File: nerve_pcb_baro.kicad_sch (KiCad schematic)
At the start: 5 parts, among them U4 BMP390

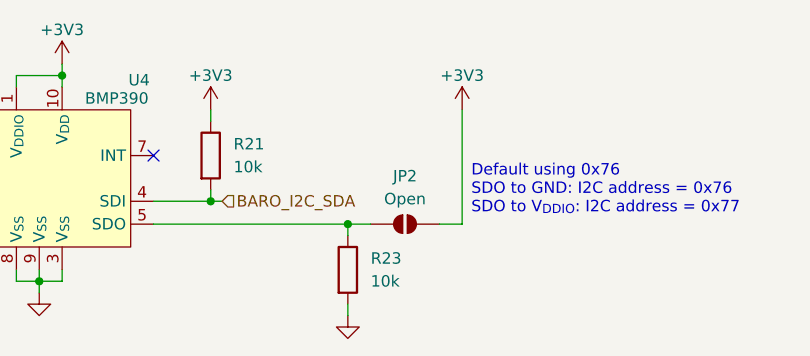
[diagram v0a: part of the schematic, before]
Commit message: Cleanup Vbatt circuit and fix silkscreen
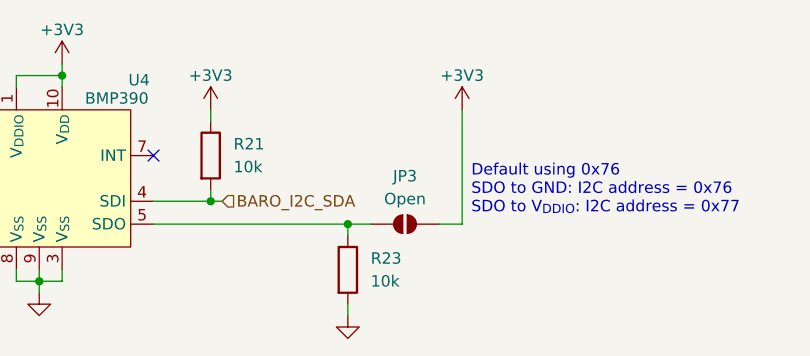
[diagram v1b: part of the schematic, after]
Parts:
- renumbered JP2 to JP3
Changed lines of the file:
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@@
 		(dnp no)
 		(fields_autoplaced yes)
-		(property "Reference" "#PWR074"
+		(property "Reference" "#PWR076"
 			(at 137.16 115.57 0)
 			(effects
@@
 			(project "nerve_pcb"
 				(path "/c0277862-b3f2-4e0e-986f-34702f0543f0/9de129d2-0f7b-4a2d-85ad-214e335f6288"
-					(reference "#PWR074")
+					(reference "#PWR076")
 					(unit 1)
 				)
@@
 		(on_board yes)
 		(dnp no)
-		(property "Reference" "#PWR071"
+		(property "Reference" "#PWR073"
 			(at 184.15 92.71 0)
 			(effects
@@
 			(project "nerve_pcb"
 				(path "/c0277862-b3f2-4e0e-986f-34702f0543f0/9de129d2-0f7b-4a2d-85ad-214e335f6288"
-					(reference "#PWR071")
+					(reference "#PWR073")
 					(unit 1)
 				)
@@
 		(on_board yes)
 		(dnp no)
-		(property "Reference" "#PWR070"
+		(property "Reference" "#PWR072"
 			(at 156.21 92.71 0)
 			(effects
@@
 			(project "nerve_pcb"
 				(path "/c0277862-b3f2-4e0e-986f-34702f0543f0/9de129d2-0f7b-4a2d-85ad-214e335f6288"
-					(reference "#PWR070")
+					(reference "#PWR072")
 					(unit 1)
 				)
@@
 		(on_board yes)
 		(dnp no)
-		(property "Reference" "JP2"
+		(property "Reference" "JP3"
 			(at 177.8 96.266 0)
 			(effects
@@
 			(project "nerve_pcb"
 				(path "/c0277862-b3f2-4e0e-986f-34702f0543f0/9de129d2-0f7b-4a2d-85ad-214e335f6288"
-					(reference "JP2")
+					(reference "JP3")
 					(unit 1)
 				)
@@
 		(on_board yes)
 		(dnp no)
-		(property "Reference" "#PWR069"
+		(property "Reference" "#PWR071"
 			(at 139.7 87.63 0)
 			(effects
@@
 			(project "nerve_pcb"
 				(path "/c0277862-b3f2-4e0e-986f-34702f0543f0/9de129d2-0f7b-4a2d-85ad-214e335f6288"
-					(reference "#PWR069")
+					(reference "#PWR071")
 					(unit 1)
 				)
@@
 		(on_board yes)
 		(dnp no)
-		(property "Reference" "#PWR072"
+		(property "Reference" "#PWR074"
 			(at 123.19 96.52 0)
 			(effects
@@
 			(project "nerve_pcb"
 				(path "/c0277862-b3f2-4e0e-986f-34702f0543f0/9de129d2-0f7b-4a2d-85ad-214e335f6288"
-					(reference "#PWR072")
+					(reference "#PWR074")
 					(unit 1)
 				)
@@
 		(on_board yes)
 		(dnp no)
-		(property "Reference" "#PWR073"
+		(property "Reference" "#PWR075"
 			(at 114.3 100.33 0)
 			(effects
@@
 			(project "nerve_pcb"
 				(path "/c0277862-b3f2-4e0e-986f-34702f0543f0/9de129d2-0f7b-4a2d-85ad-214e335f6288"
-					(reference "#PWR073")
+					(reference "#PWR075")
 					(unit 1)
 				)
@@
 		(dnp no)
 		(fields_autoplaced yes)
-		(property "Reference" "#PWR075"
+		(property "Reference" "#PWR077"
 			(at 171.45 118.11 0)
 			(effects
@@
 			(project "nerve_pcb"
 				(path "/c0277862-b3f2-4e0e-986f-34702f0543f0/9de129d2-0f7b-4a2d-85ad-214e335f6288"
-					(reference "#PWR075")
-					(unit 1)
-				)
+					(reference "#PWR077")
+					(unit 1)
+				)

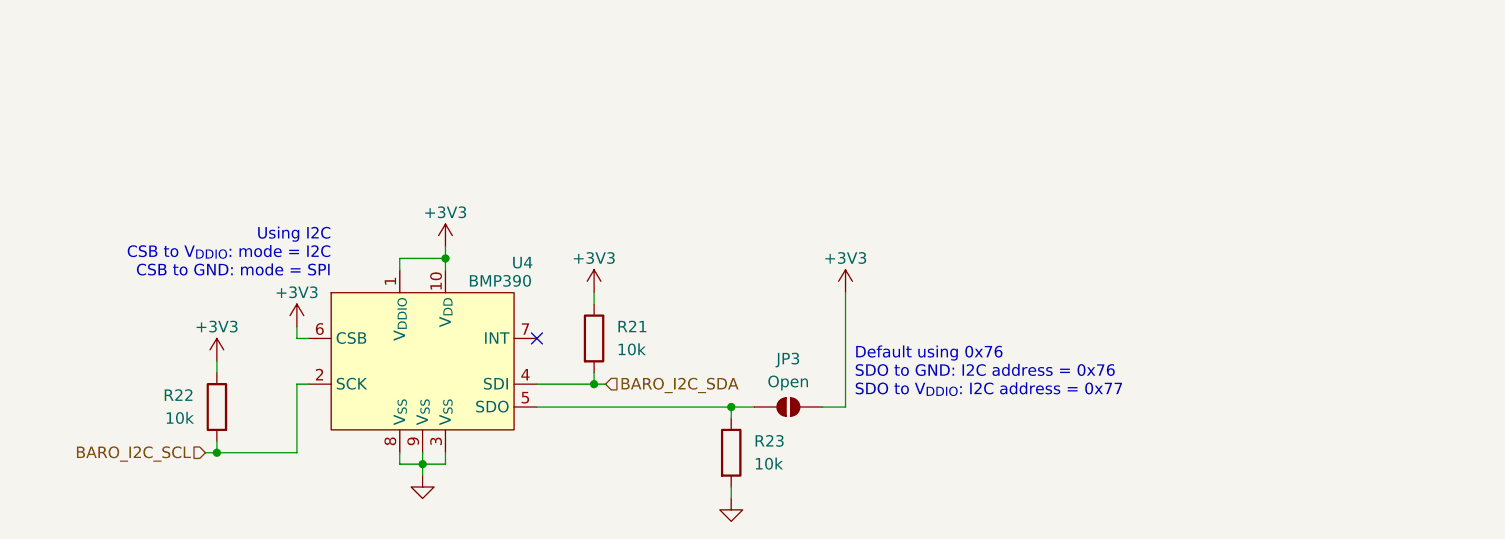
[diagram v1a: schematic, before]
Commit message: Schematic corrections
- Add decoupling caps for sensor ICs
- Fix clock circuits
- Add BNO085 clock jumper
- Minor cleanup
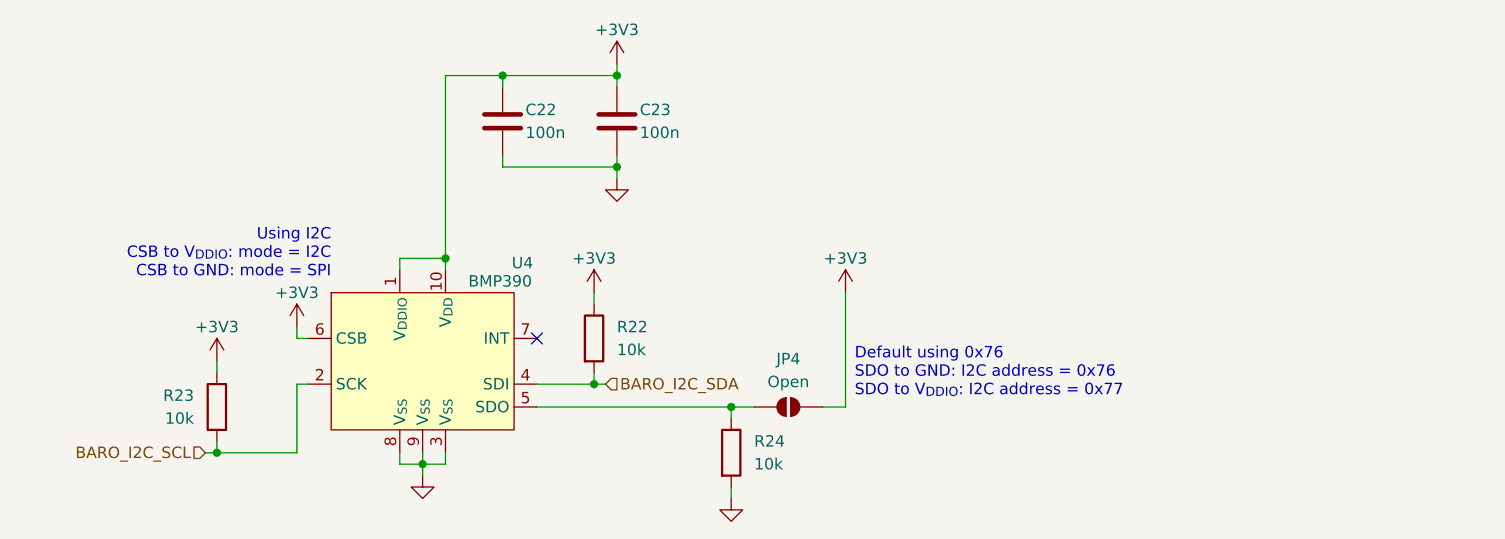
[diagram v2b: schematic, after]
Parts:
- added C22, C23: 100n, Capacitor_SMD:C_0603_1608Metric, symbol Device:C
- renumbered JP3 to JP4, R21 to R22, R22 to R23, R23 to R24
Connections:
- net +3V3: now also C22.1, C23.1
- net GND: now also C22.2, C23.2

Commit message: Simplify clock circuits
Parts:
- renumbered R22 to R19, R23 to R20, R24 to R21
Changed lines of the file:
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@@
 		(on_board yes)
 		(dnp no)
-		(property "Reference" "R22"
+		(property "Reference" "R19"
 			(at 158.75 92.7099 0)
 			(effects
@@
 			(project "nerve_pcb"
 				(path "/c0277862-b3f2-4e0e-986f-34702f0543f0/9de129d2-0f7b-4a2d-85ad-214e335f6288"
-					(reference "R22")
+					(reference "R19")
 					(unit 1)
 				)
@@
 		(on_board yes)
 		(dnp no)
-		(property "Reference" "R23"
+		(property "Reference" "R20"
 			(at 111.76 100.3299 0)
 			(effects
@@
 			(project "nerve_pcb"
 				(path "/c0277862-b3f2-4e0e-986f-34702f0543f0/9de129d2-0f7b-4a2d-85ad-214e335f6288"
-					(reference "R23")
+					(reference "R20")
 					(unit 1)
 				)
@@
 		(on_board yes)
 		(dnp no)
-		(property "Reference" "R24"
+		(property "Reference" "R21"
 			(at 173.99 105.4099 0)
 			(effects
@@
 			(project "nerve_pcb"
 				(path "/c0277862-b3f2-4e0e-986f-34702f0543f0/9de129d2-0f7b-4a2d-85ad-214e335f6288"
-					(reference "R24")
-					(unit 1)
-				)
+					(reference "R21")
+					(unit 1)
+				)

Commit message: Update IMU clock circuit and cleanup
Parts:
- renumbered R19 to R17, R20 to R18, R21 to R19
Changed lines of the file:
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@@
 		(on_board yes)
 		(dnp no)
-		(property "Reference" "R19"
+		(property "Reference" "R17"
 			(at 158.75 92.7099 0)
 			(effects
@@
 			(project "nerve_pcb"
 				(path "/c0277862-b3f2-4e0e-986f-34702f0543f0/9de129d2-0f7b-4a2d-85ad-214e335f6288"
-					(reference "R19")
+					(reference "R17")
 					(unit 1)
 				)
@@
 		(on_board yes)
 		(dnp no)
-		(property "Reference" "R20"
+		(property "Reference" "R18"
 			(at 111.76 100.3299 0)
 			(effects
@@
 			(project "nerve_pcb"
 				(path "/c0277862-b3f2-4e0e-986f-34702f0543f0/9de129d2-0f7b-4a2d-85ad-214e335f6288"
-					(reference "R20")
+					(reference "R18")
 					(unit 1)
 				)
@@
 		(on_board yes)
 		(dnp no)
-		(property "Reference" "R21"
+		(property "Reference" "R19"
 			(at 173.99 105.4099 0)
 			(effects
@@
 			(project "nerve_pcb"
 				(path "/c0277862-b3f2-4e0e-986f-34702f0543f0/9de129d2-0f7b-4a2d-85ad-214e335f6288"
-					(reference "R21")
-					(unit 1)
-				)
+					(reference "R19")
+					(unit 1)
+				)

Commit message: Add WS2812Bs
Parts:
- renumbered U4 to U5
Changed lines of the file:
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@@
 		(dnp no)
 		(fields_autoplaced yes)
-		(property "Reference" "#PWR069"
+		(property "Reference" "#PWR076"
 			(at 137.16 115.57 0)
 			(effects
@@
 			(project "nerve_pcb"
 				(path "/c0277862-b3f2-4e0e-986f-34702f0543f0/9de129d2-0f7b-4a2d-85ad-214e335f6288"
-					(reference "#PWR069")
+					(reference "#PWR076")
 					(unit 1)
 				)
@@
 		(on_board yes)
 		(dnp no)
-		(property "Reference" "#PWR066"
+		(property "Reference" "#PWR073"
 			(at 184.15 92.71 0)
 			(effects
@@
 			(project "nerve_pcb"
 				(path "/c0277862-b3f2-4e0e-986f-34702f0543f0/9de129d2-0f7b-4a2d-85ad-214e335f6288"
-					(reference "#PWR066")
+					(reference "#PWR073")
 					(unit 1)
 				)
@@
 		(on_board yes)
 		(dnp no)
-		(property "Reference" "#PWR065"
+		(property "Reference" "#PWR072"
 			(at 156.21 92.71 0)
 			(effects
@@
 			(project "nerve_pcb"
 				(path "/c0277862-b3f2-4e0e-986f-34702f0543f0/9de129d2-0f7b-4a2d-85ad-214e335f6288"
-					(reference "#PWR065")
+					(reference "#PWR072")
 					(unit 1)
 				)
@@
 		(on_board yes)
 		(dnp no)
-		(property "Reference" "U4"
+		(property "Reference" "U5"
 			(at 147.066 85.598 0)
 			(effects
@@
 			(project ""
 				(path "/c0277862-b3f2-4e0e-986f-34702f0543f0/9de129d2-0f7b-4a2d-85ad-214e335f6288"
-					(reference "U4")
+					(reference "U5")
 					(unit 1)
 				)
@@
 		(on_board yes)
 		(dnp no)
-		(property "Reference" "#PWR063"
+		(property "Reference" "#PWR070"
 			(at 158.75 67.31 0)
 			(effects
@@
 			(project "nerve_pcb"
 				(path "/c0277862-b3f2-4e0e-986f-34702f0543f0/9de129d2-0f7b-4a2d-85ad-214e335f6288"
-					(reference "#PWR063")
+					(reference "#PWR070")
 					(unit 1)
 				)
@@
 		(dnp no)
 		(fields_autoplaced yes)
-		(property "Reference" "#PWR064"
+		(property "Reference" "#PWR071"
 			(at 158.75 82.55 0)
 			(effects
@@
 			(project "nerve_pcb"
 				(path "/c0277862-b3f2-4e0e-986f-34702f0543f0/9de129d2-0f7b-4a2d-85ad-214e335f6288"
-					(reference "#PWR064")
+					(reference "#PWR071")
 					(unit 1)
 				)
@@
 		(on_board yes)
 		(dnp no)
-		(property "Reference" "#PWR067"
+		(property "Reference" "#PWR074"
 			(at 123.19 96.52 0)
 			(effects
@@
 			(project "nerve_pcb"
 				(path "/c0277862-b3f2-4e0e-986f-34702f0543f0/9de129d2-0f7b-4a2d-85ad-214e335f6288"
-					(reference "#PWR067")
+					(reference "#PWR074")
 					(unit 1)
 				)
@@
 		(on_board yes)
 		(dnp no)
-		(property "Reference" "#PWR068"
+		(property "Reference" "#PWR075"
 			(at 114.3 100.33 0)
 			(effects
@@
 			(project "nerve_pcb"
 				(path "/c0277862-b3f2-4e0e-986f-34702f0543f0/9de129d2-0f7b-4a2d-85ad-214e335f6288"
-					(reference "#PWR068")
+					(reference "#PWR075")
 					(unit 1)
 				)
@@
 		(dnp no)
 		(fields_autoplaced yes)
-		(property "Reference" "#PWR070"
+		(property "Reference" "#PWR077"
 			(at 171.45 118.11 0)
 			(effects
@@
 			(project "nerve_pcb"
 				(path "/c0277862-b3f2-4e0e-986f-34702f0543f0/9de129d2-0f7b-4a2d-85ad-214e335f6288"
-					(reference "#PWR070")
-					(unit 1)
-				)
+					(reference "#PWR077")
+					(unit 1)
+				)

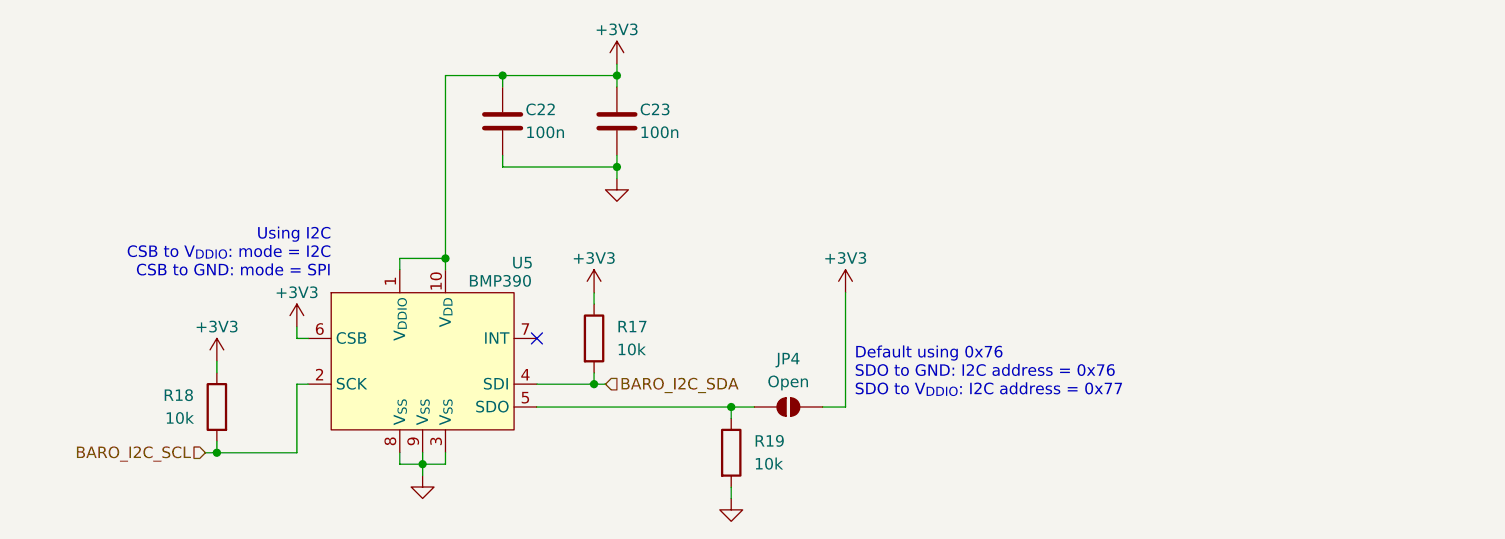
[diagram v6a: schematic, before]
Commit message: Add design notes on schematic
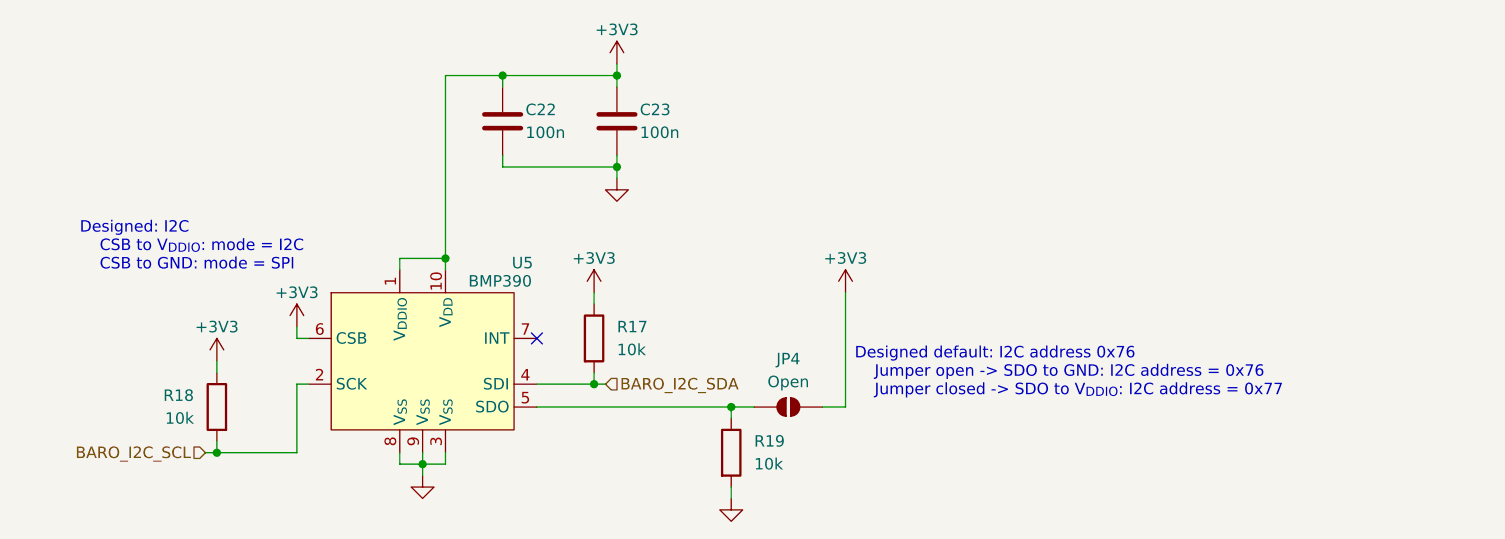
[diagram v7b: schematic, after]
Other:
- note added: "Designed default: I2C address 0x76 Jumper open -> SDO to GND: I2C address = 0x76 Jumper closed -> SDO to V_{DDIO}: I2C address = 0x77"
- note added: "Designed: I2C CSB to V_{DDIO}: mode = I2C CSB to GND: mode = SPI"
- note removed: "Default using 0x76 SDO to GND: I2C address = 0x76 SDO to V_{DDIO}: I2C address = 0x77"
- note removed: "Using I2C CSB to V_{DDIO}: mode = I2C CSB to GND: mode = SPI"
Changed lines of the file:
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@@
 		)
 	)
-	(text "Default using 0x76\nSDO to GND: I2C address = 0x76\nSDO to V_{DDIO}: I2C address = 0x77"
+	(text "Designed default: I2C address 0x76\n    Jumper open -> SDO to GND: I2C address = 0x76\n    Jumper closed -> SDO to V_{DDIO}: I2C address = 0x77"
 		(exclude_from_sim no)
 		(at 185.166 97.79 0)
@@
 		)
 	)
-	(text "Using I2C\nCSB to V_{DDIO}: mode = I2C\nCSB to GND: mode = SPI"
+	(text "Designed: I2C\n    CSB to V_{DDIO}: mode = I2C\n    CSB to GND: mode = SPI"
 		(exclude_from_sim no)
-		(at 127 84.582 0)
+		(at 99.06 83.82 0)
 		(effects
 			(font
@@
 				(thickness 0.1588)
 			)
-			(justify right)
+			(justify left)
 		)
 	)

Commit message: Fix BNO085 circuit for SPI
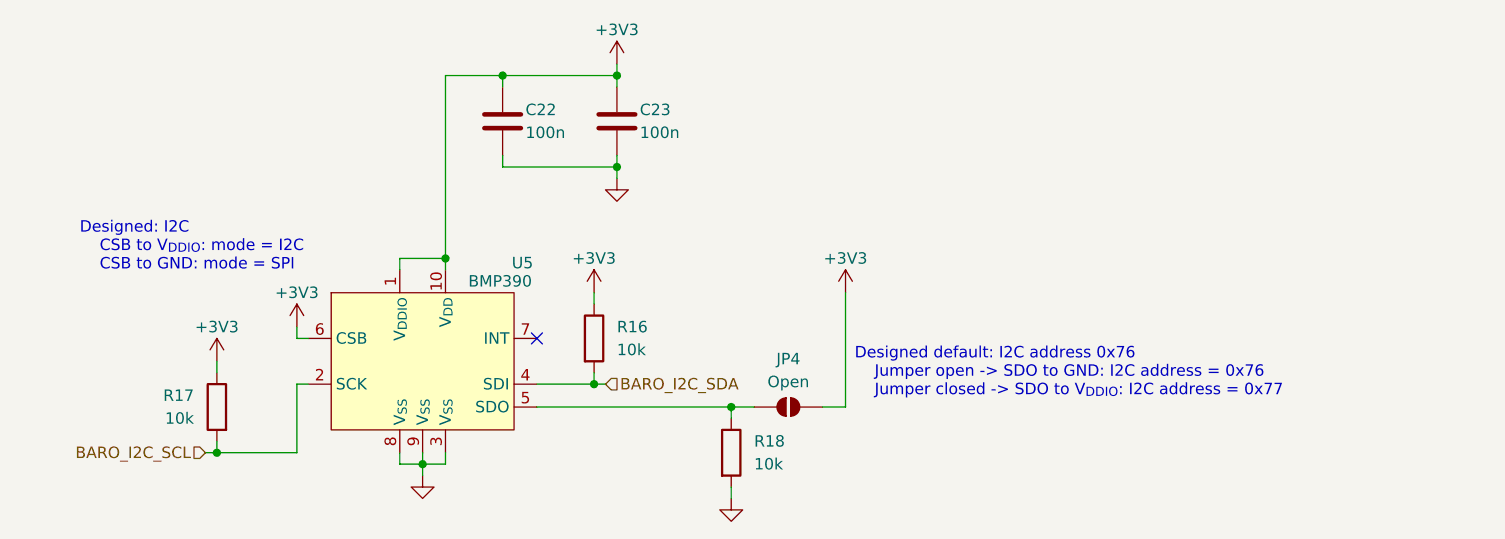
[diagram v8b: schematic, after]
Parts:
- renumbered R17 to R16, R18 to R17, R19 to R18
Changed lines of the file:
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@@
 		(dnp no)
 		(fields_autoplaced yes)
-		(property "Reference" "#PWR076"
+		(property "Reference" "#PWR075"
 			(at 137.16 115.57 0)
 			(effects
@@
 			(project "nerve_pcb"
 				(path "/c0277862-b3f2-4e0e-986f-34702f0543f0/9de129d2-0f7b-4a2d-85ad-214e335f6288"
-					(reference "#PWR076")
+					(reference "#PWR075")
 					(unit 1)
 				)
@@
 		(on_board yes)
 		(dnp no)
-		(property "Reference" "#PWR073"
+		(property "Reference" "#PWR072"
 			(at 184.15 92.71 0)
 			(effects
@@
 			(project "nerve_pcb"
 				(path "/c0277862-b3f2-4e0e-986f-34702f0543f0/9de129d2-0f7b-4a2d-85ad-214e335f6288"
-					(reference "#PWR073")
+					(reference "#PWR072")
 					(unit 1)
 				)
@@
 		(on_board yes)
 		(dnp no)
-		(property "Reference" "#PWR072"
+		(property "Reference" "#PWR071"
 			(at 156.21 92.71 0)
 			(effects
@@
 			(project "nerve_pcb"
 				(path "/c0277862-b3f2-4e0e-986f-34702f0543f0/9de129d2-0f7b-4a2d-85ad-214e335f6288"
-					(reference "#PWR072")
+					(reference "#PWR071")
 					(unit 1)
 				)
@@
 		(on_board yes)
 		(dnp no)
-		(property "Reference" "R17"
+		(property "Reference" "R16"
 			(at 158.75 92.7099 0)
 			(effects
@@
 			(project "nerve_pcb"
 				(path "/c0277862-b3f2-4e0e-986f-34702f0543f0/9de129d2-0f7b-4a2d-85ad-214e335f6288"
-					(reference "R17")
+					(reference "R16")
 					(unit 1)
 				)
@@
 		(on_board yes)
 		(dnp no)
-		(property "Reference" "R18"
+		(property "Reference" "R17"
 			(at 111.76 100.3299 0)
 			(effects
@@
 			(project "nerve_pcb"
 				(path "/c0277862-b3f2-4e0e-986f-34702f0543f0/9de129d2-0f7b-4a2d-85ad-214e335f6288"
-					(reference "R18")
+					(reference "R17")
 					(unit 1)
 				)
@@
 		(on_board yes)
 		(dnp no)
-		(property "Reference" "#PWR070"
+		(property "Reference" "#PWR069"
 			(at 158.75 67.31 0)
 			(effects
@@
 			(project "nerve_pcb"
 				(path "/c0277862-b3f2-4e0e-986f-34702f0543f0/9de129d2-0f7b-4a2d-85ad-214e335f6288"
-					(reference "#PWR070")
+					(reference "#PWR069")
 					(unit 1)
 				)
@@
 		(dnp no)
 		(fields_autoplaced yes)
-		(property "Reference" "#PWR071"
+		(property "Reference" "#PWR070"
 			(at 158.75 82.55 0)
 			(effects
@@
 			(project "nerve_pcb"
 				(path "/c0277862-b3f2-4e0e-986f-34702f0543f0/9de129d2-0f7b-4a2d-85ad-214e335f6288"
-					(reference "#PWR071")
+					(reference "#PWR070")
 					(unit 1)
 				)
@@
 		(on_board yes)
 		(dnp no)
-		(property "Reference" "#PWR074"
+		(property "Reference" "#PWR073"
 			(at 123.19 96.52 0)
 			(effects
@@
 			(project "nerve_pcb"
 				(path "/c0277862-b3f2-4e0e-986f-34702f0543f0/9de129d2-0f7b-4a2d-85ad-214e335f6288"
-					(reference "#PWR074")
+					(reference "#PWR073")
 					(unit 1)
 				)
@@
 		(on_board yes)
 		(dnp no)
-		(property "Reference" "R19"
+		(property "Reference" "R18"
 			(at 173.99 105.4099 0)
 			(effects
@@
 			(project "nerve_pcb"
 				(path "/c0277862-b3f2-4e0e-986f-34702f0543f0/9de129d2-0f7b-4a2d-85ad-214e335f6288"
-					(reference "R19")
+					(reference "R18")
 					(unit 1)
 				)
@@
 		(on_board yes)
 		(dnp no)
-		(property "Reference" "#PWR075"
+		(property "Reference" "#PWR074"
 			(at 114.3 100.33 0)
 			(effects
@@
 			(project "nerve_pcb"
 				(path "/c0277862-b3f2-4e0e-986f-34702f0543f0/9de129d2-0f7b-4a2d-85ad-214e335f6288"
-					(reference "#PWR075")
+					(reference "#PWR074")
 					(unit 1)
 				)
@@
 		(dnp no)
 		(fields_autoplaced yes)
-		(property "Reference" "#PWR077"
+		(property "Reference" "#PWR076"
 			(at 171.45 118.11 0)
 			(effects
@@
 			(project "nerve_pcb"
 				(path "/c0277862-b3f2-4e0e-986f-34702f0543f0/9de129d2-0f7b-4a2d-85ad-214e335f6288"
-					(reference "#PWR077")
-					(unit 1)
-				)
+					(reference "#PWR076")
+					(unit 1)
+				)
